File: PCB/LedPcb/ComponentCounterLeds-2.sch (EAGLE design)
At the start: 13 parts

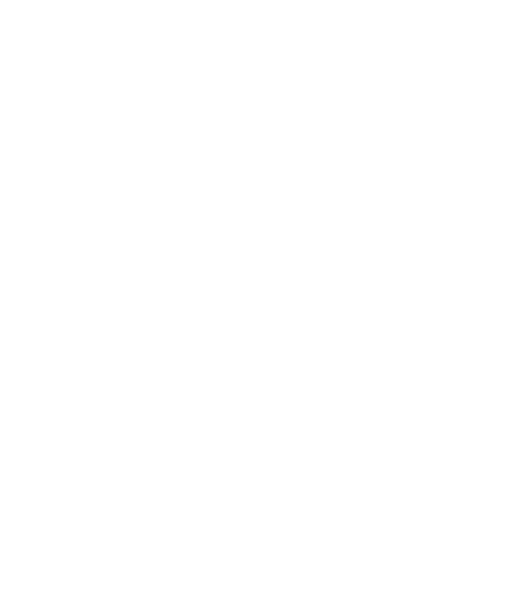
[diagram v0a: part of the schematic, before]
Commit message: Changed each spool block width to 15mm to give more space for the spools.
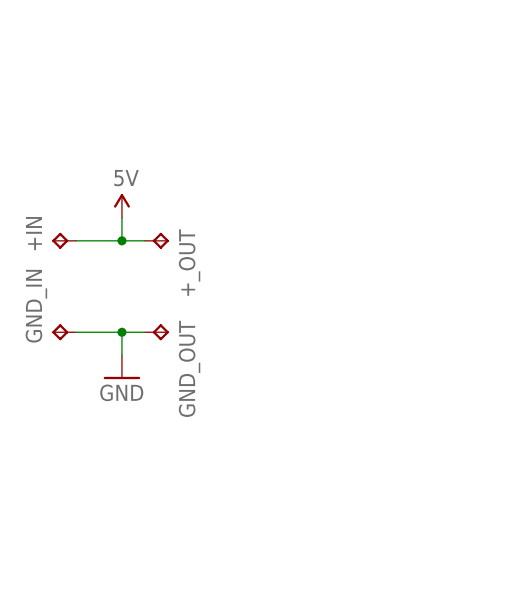
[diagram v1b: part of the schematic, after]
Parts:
- added +IN, +_OUT, GND_IN, GND_OUT: TPTP15R, testpad:TPTP15R
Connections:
- net 5V: now also +IN.TP, +_OUT.TP
- net GND: now also GND_IN.TP, GND_OUT.TP
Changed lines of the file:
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@@
 <part name="R3" library="SparkFun-Resistors" deviceset="RESISTOR" device="1206" value="300R"/>
 <part name="R4" library="SparkFun-Resistors" deviceset="RESISTOR" device="1206" value="300R"/>
+<part name="+IN" library="testpad" deviceset="TP" device="TP15R"/>
+<part name="+_OUT" library="testpad" deviceset="TP" device="TP15R"/>
+<part name="GND_IN" library="testpad" deviceset="TP" device="TP15R"/>
+<part name="GND_OUT" library="testpad" deviceset="TP" device="TP15R"/>
+<part name="SUPPLY3" library="SparkFun-Aesthetics" deviceset="5V" device=""/>
+<part name="GND3" library="SparkFun-Aesthetics" deviceset="GND" device=""/>
 </parts>
 <sheets>
@@
 <instance part="R3" gate="G$1" x="22.86" y="20.32" rot="R90"/>
 <instance part="R4" gate="G$1" x="43.18" y="20.32" rot="R90"/>
+<instance part="+IN" gate="G$1" x="-45.72" y="25.4" rot="R90"/>
+<instance part="+_OUT" gate="G$1" x="-33.02" y="25.4" rot="R270"/>
+<instance part="GND_IN" gate="G$1" x="-45.72" y="15.24" rot="R90"/>
+<instance part="GND_OUT" gate="G$1" x="-33.02" y="15.24" rot="R270"/>
+<instance part="SUPPLY3" gate="G$1" x="-38.1" y="27.94"/>
+<instance part="GND3" gate="1" x="-38.1" y="10.16"/>
 </instances>
 <busses>
@@
 <pinref part="SUPPLY2" gate="G$1" pin="5V"/>
 </segment>
+<segment>
+<pinref part="+IN" gate="G$1" pin="TP"/>
+<pinref part="+_OUT" gate="G$1" pin="TP"/>
+<wire x1="-43.18" y1="25.4" x2="-38.1" y2="25.4" width="0.1524" layer="91"/>
+<wire x1="-38.1" y1="25.4" x2="-35.56" y2="25.4" width="0.1524" layer="91"/>
+<wire x1="-38.1" y1="25.4" x2="-38.1" y2="27.94" width="0.1524" layer="91"/>
+<pinref part="SUPPLY3" gate="G$1" pin="5V"/>
+<junction x="-38.1" y="25.4"/>
+</segment>
 </net>
 <net name="GND" class="0">
@@
 <wire x1="76.2" y1="45.72" x2="76.2" y2="48.26" width="0.1524" layer="91"/>
 </segment>
+<segment>
+<pinref part="GND_OUT" gate="G$1" pin="TP"/>
+<pinref part="GND_IN" gate="G$1" pin="TP"/>
+<wire x1="-35.56" y1="15.24" x2="-38.1" y2="15.24" width="0.1524" layer="91"/>
+<wire x1="-38.1" y1="15.24" x2="-43.18" y2="15.24" width="0.1524" layer="91"/>
+<wire x1="-38.1" y1="15.24" x2="-38.1" y2="12.7" width="0.1524" layer="91"/>
+<pinref part="GND3" gate="1" pin="GND"/>
+<junction x="-38.1" y="15.24"/>
+</segment>
 </net>
